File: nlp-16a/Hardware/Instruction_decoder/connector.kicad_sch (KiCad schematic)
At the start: 0 parts

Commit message: 命令デコーダ ロジック部の設計だいたい完了git statusgit statusやったぜ
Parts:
- added J? (x2): Conn_02x10_Odd_Even, Connector_PinHeader_2.54mm:PinHeader_2x10_P2.54mm_Horizontal, symbol Connector_Generic:Conn_02x10_Odd_Even
- added J? (x2): Conn_02x10_Counter_Clockwise, Connector_PinHeader_2.54mm:PinHeader_2x10_P2.54mm_Horizontal, symbol Connector_Generic:Conn_02x10_Odd_Even
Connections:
- new net 3word: J?.20 (Pin_20)
- new net ALL_CLK: J?.14 (Pin_14)
- new net A_BUS_Addr0: J?.2 (Pin_2), J?.20 (Pin_20)
- new net A_BUS_Addr1: J?.18 (Pin_18), J?.4 (Pin_4)
- new net A_BUS_Addr2: J?.16 (Pin_16), J?.6 (Pin_6)
- new net A_BUS_Addr3: J?.14 (Pin_14), J?.8 (Pin_8)
- new net BUS_A/~{B}: J?.9 (Pin_9)
- new net BUS_A/~{Y}: J?.7 (Pin_7)
- new net Fetch: J?.11 (Pin_11)
- new net GND: J?.16 (Pin_16), J?.16 (Pin_16), J?.18 (Pin_18), J?.18 (Pin_18), J?.20 (Pin_20), J?.20 (Pin_20)
- new net INT: J?.16 (Pin_16)
- new net OP0: J?.19 (Pin_19)
- new net OP1: J?.17 (Pin_17)
- new net OP2: J?.15 (Pin_15)
- new net OP3: J?.13 (Pin_13)
- new net OP4: J?.11 (Pin_11)
- new net OP5: J?.9 (Pin_9)
- new net OP6: J?.7 (Pin_7)
- new net OP7: J?.5 (Pin_5)
- new net RS: J?.14 (Pin_14)
- new net Seed_pluse: J?.12 (Pin_12)
- new net Y_BUS_Addr0: J?.12 (Pin_12), J?.2 (Pin_2)
- new net Y_BUS_Addr1: J?.10 (Pin_10), J?.4 (Pin_4)
- new net Y_BUS_Addr2: J?.6 (Pin_6), J?.8 (Pin_8)
- new net Y_BUS_Addr3: J?.6 (Pin_6), J?.8 (Pin_8)
- new net Y_Flag_sel: J?.13 (Pin_13)
- new net phi1: J?.12 (Pin_12)
- new net phi2: J?.10 (Pin_10)
- new net ~{Acc_Y}: J?.13 (Pin_13)
- new net ~{Address_Y}: J?.5 (Pin_5)
- new net ~{DEC_ALU}: J?.15 (Pin_15)
- new net ~{Flag_A}: J?.9 (Pin_9)
- new net ~{Flag_Y}: J?.9 (Pin_9)
- new net ~{INC_ALU}: J?.17 (Pin_17)
- new net ~{INTERNAL_ALU}: J?.19 (Pin_19)
- new net ~{INTERNAL_A}: J?.19 (Pin_19)
- new net ~{INTERNAL_Y}: J?.19 (Pin_19)
- new net ~{IP_A}: J?.3 (Pin_3)
- new net ~{IP_Y}: J?.3 (Pin_3)
- new net ~{IR1_Y}: J?.17 (Pin_17)
- new net ~{IR2_Y}: J?.15 (Pin_15)
- new net ~{IR3_Y}: J?.11 (Pin_11)
- new net ~{IV_A}: J?.13 (Pin_13)
- new net ~{MEM_A}: J?.7 (Pin_7)
- new net ~{MEM_Y}: J?.7 (Pin_7)
- new net ~{NOP}: J?.18 (Pin_18)
- new net ~{SP_A}: J?.1 (Pin_1)
- new net ~{SP_Y}: J?.1 (Pin_1)
- no-connect marks 0 -> 7
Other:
- note added: "YバスではΦ1，Φ2で使用する"
- note added: "Yバスでは全レジスタ指定で使用する"

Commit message: アノテーションまで完了．基板設計に入る
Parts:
- added C1, C10, C11, C12, C13, C14, C15, C16, C17, C18, C19, C2, C20, C21, C22, C23, C3, C4, C5, C6, C8, C9: C, Capacitor_THT:C_Disc_D7.5mm_W2.5mm_P5.00mm, symbol Device:C
- added C7: C_Polarized, Capacitor_THT:CP_Radial_D5.0mm_P2.50mm, symbol Device:C_Polarized
- added D1: LED, LED_THT:LED_D3.0mm, symbol Device:LED
- added H1, H2, H3, H4: MountingHole_Pad, MountingHole:MountingHole_3mm_Pad, symbol Mechanical:MountingHole_Pad
- added J3: Screw_Terminal_01x02, TerminalBlock:TerminalBlock_bornier-2_P5.08mm, symbol Connector:Screw_Terminal_01x02
- added R1: R, Resistor_SMD:R_0603_1608Metric_Pad0.98x0.95mm_HandSolder, symbol Device:R
- added U85: CD74HC00, Package_DIP:DIP-14_W7.62mm, symbol CD74HCXX:CD74HC00
- gave numbers to parts that had none: 4
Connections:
- net RS is gone; now on net ~{RS}: J2.14 (Pin_14)
- net ~{Acc_Y} is gone; now on net ~{IR3_Y}: J4.13 (Pin_13)
- net GND: now also J1.2 (Pin_2), J1.4 (Pin_4), J2.2 (Pin_2), J2.4 (Pin_4), C1.1, C10.1, C11.1, C12.1, C13.1, C14.1, C15.1, C16.1, C17.1, C18.1, C19.1, C2.1, C20.1, C21.1, C22.1, C23.1, C3.1, C4.1, C5.1, C6.1, C7.2, C8.1, C9.1, H1.1, H2.1, H3.1, H4.1, J3.1 (Pin_1), R1.2, U85.4, U85.5, U85.7 (GND), U85.7 (GND), U85.7 (GND), U85.7 (GND)
- net phi1: now also J2.10 (Pin_10)
- net phi2: now also J2.8 (Pin_8), U85.12; no longer J4.10 (Pin_10)
- net ~{IR3_Y}: no longer J4.11 (Pin_11)
- net ALL_CLK renamed ~{RS}
- net BUS_A/~{B} renamed ~{RA3}
- net BUS_A/~{Y} renamed ~{RAM_STORE->}
- net Fetch renamed ~{Fetch_Status}
- net ~{Fetch_Status}: now also U85.1
- net Seed_pluse renamed ~{Seed_pluse}
- net ~{Flag_A} renamed ~{Flag_SAVE->}
- net ~{IV_A} renamed ~{IV_JMP->}
- net ~{NOP} renamed NOP
- net NOP: now also U85.2
- new net: D1.1 (K), R1.1
- new net: U85.13, U85.3
- new net: U85.10, U85.11, U85.9
- new net Reg_pulse: J4.10 (Pin_10), U85.8
- new net VCC: C1.2, C10.2, C11.2, C12.2, C13.2, C14.2, C15.2, C16.2, C17.2, C18.2, C19.2, C2.2, C20.2, C21.2, C22.2, C23.2, C3.2, C4.2, C5.2, C6.2, C7.1, C8.2, C9.2, D1.2 (A), J3.2 (Pin_2), U85.14 (VCC), U85.14 (VCC), U85.14 (VCC), U85.14 (VCC)
- no-connect marks 7 -> 15
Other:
- note added: "BUS_A/~{B}"
- note added: "BUS_A/~{Y}"
- note added: "Power"

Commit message: 基板設計 今日はとりあえずここまで
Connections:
- net 3word: now also J2.12 (Pin_12); no longer J2.20 (Pin_20)
- net A_BUS_Addr0: now also J1.12 (Pin_12); no longer J1.20 (Pin_20)
- net A_BUS_Addr1: now also J1.10 (Pin_10); no longer J1.18 (Pin_18)
- net A_BUS_Addr2: now also J1.8 (Pin_8); no longer J1.16 (Pin_16)
- net A_BUS_Addr3: now also J1.6 (Pin_6); no longer J1.14 (Pin_14)
- net INT: now also J2.10 (Pin_10); no longer J2.16 (Pin_16)
- net NOP: now also J2.16 (Pin_16); no longer J2.18 (Pin_18)
- net Y_BUS_Addr0: now also J1.20 (Pin_20); no longer J1.12 (Pin_12)
- net Y_BUS_Addr1: now also J1.18 (Pin_18); no longer J1.10 (Pin_10)
- net Y_BUS_Addr2: now also J1.16 (Pin_16); no longer J1.8 (Pin_8)
- net Y_BUS_Addr3: now also J1.14 (Pin_14); no longer J1.6 (Pin_6)
- net phi1: now also J2.20 (Pin_20); no longer J2.10 (Pin_10)
- net phi2: now also J2.18 (Pin_18); no longer J2.8 (Pin_8)
- net ~{Seed_pluse}: now also J2.8 (Pin_8); no longer J2.12 (Pin_12)

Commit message: 基板設計 進捗
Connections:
- net 3word: now also J2.8 (Pin_8); no longer J2.12 (Pin_12)
- net ~{IR3_Y}: now also J4.11 (Pin_11); no longer J4.13 (Pin_13)
- net ~{Seed_pluse}: now also J2.12 (Pin_12); no longer J2.8 (Pin_8)
- new net Acc_Y: J4.13 (Pin_13)
- no-connect marks 15 -> 14
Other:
- note added: "Accだけは正論理"
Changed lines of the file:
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@@
   (junction (at 168.91 142.24) (diameter 0) (color 0 0 0 0)
   )
-  (no_connect (at 228.6 45.72))
   (no_connect (at 142.24 121.92))
   (no_connect (at 73.66 87.63))
@@
     (effects (font (size 1.27 1.27)) (justify left bottom))
   )
+  (text "Accだけは正論理" (at 237.49 44.45 0)
+    (effects (font (size 1.27 1.27)) (justify left bottom))
+  )
   (text "BUS_A/~{B}" (at 104.14 83.82 0)
     (effects (font (size 1.27 1.27)) (justify left bottom))
@@
     )
   )
-  (global_label "~{Seed_pluse}" (shape output) (at 62.23 85.09 180) (fields_autoplaced)
-    (effects (font (size 1.27 1.27)) (justify right))
-    (property "Intersheet References" "${INTERSHEET_REFS}" (id 0) (at 49.2336 85.0106 0)
+  (global_label "~{Seed_pluse}" (shape output) (at 62.23 80.01 180) (fields_autoplaced)
+    (effects (font (size 1.27 1.27)) (justify right))
+    (property "Intersheet References" "${INTERSHEET_REFS}" (id 0) (at 49.2336 79.9306 0)
       (effects (font (size 1.27 1.27)) (justify right) hide)
     )
@@
     )
   )
-  (global_label "~{IR3_Y}" (shape input) (at 228.6 43.18 0) (fields_autoplaced)
-    (effects (font (size 1.27 1.27)) (justify left))
-    (property "Intersheet References" "${INTERSHEET_REFS}" (id 0) (at 236.1536 43.1006 0)
+  (global_label "~{IR3_Y}" (shape input) (at 228.6 45.72 0) (fields_autoplaced)
+    (effects (font (size 1.27 1.27)) (justify left))
+    (property "Intersheet References" "${INTERSHEET_REFS}" (id 0) (at 236.1536 45.6406 0)
       (effects (font (size 1.27 1.27)) (justify left) hide)
     )
@@
     )
   )
+  (global_label "Acc_Y" (shape input) (at 228.6 43.18 0) (fields_autoplaced)
+    (effects (font (size 1.27 1.27)) (justify left))
+    (property "Intersheet References" "${INTERSHEET_REFS}" (id 0) (at 236.335 43.1006 0)
+      (effects (font (size 1.27 1.27)) (justify left) hide)
+    )
+  )
   (global_label "~{SP_Y}" (shape input) (at 228.6 58.42 0) (fields_autoplaced)
     (effects (font (size 1.27 1.27)) (justify left))
@@
     )
   )
-  (global_label "3word" (shape output) (at 62.23 80.01 180) (fields_autoplaced)
-    (effects (font (size 1.27 1.27)) (justify right))
-    (property "Intersheet References" "${INTERSHEET_REFS}" (id 0) (at 54.1926 79.9306 0)
-      (effects (font (size 1.27 1.27)) (justify right) hide)
-    )
+  (global_label "3word" (shape output) (at 62.23 85.09 180) (fields_autoplaced)
+    (effects (font (size 1.27 1.27)) (justify right))
+    (property "Intersheet References" "${INTERSHEET_REFS}" (id 0) (at 54.1926 85.0106 0)
+      (effects (font (size 1.27 1.27)) (justify right) hide)
+    )

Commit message: 命令デコーダ完了！！
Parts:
- added C23, C24, C25, C26, C27, C28, C29: C, Capacitor_THT:C_Disc_D7.0mm_W2.5mm_P5.00mm, symbol Device:C
- added D2: LED, LED_THT:LED_D3.0mm, symbol Device:LED
- added J6, J7, J8, J9: Conn_01x02_Female, Connector_PinSocket_2.54mm:PinSocket_1x02_P2.54mm_Vertical, symbol Connector:Conn_01x02_Female
- added R2: R, Resistor_SMD:R_0603_1608Metric_Pad0.98x0.95mm_HandSolder, symbol Device:R
- added U86, U87, U88: CD74HC00, Package_DIP:DIP-14_W7.62mm, symbol CD74HCXX:CD74HC00
- C1, C10, C11, C12, C13, C14, C15, C16, C17, C18, C19, C2, C20, C21, C22, C3, C4, C5, C6, C8, C9: footprint Capacitor_THT:C_Disc_D7.5mm_W2.5mm_P5.00mm -> Capacitor_THT:C_Disc_D7.0mm_W2.5mm_P5.00mm
- C7: renamed from C23; footprint Capacitor_THT:C_Disc_D7.5mm_W2.5mm_P5.00mm -> Capacitor_THT:C_Disc_D7.0mm_W2.5mm_P5.00mm
- renumbered C7 to C30
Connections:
- net GND: now also C23.1, C24.1, C25.1, C26.1, C27.1, C28.1, C29.1, J6.1 (Pin_1), J7.1 (Pin_1), J8.1 (Pin_1), J9.1 (Pin_1), R2.2, U86.7 (GND), U86.7 (GND), U86.7 (GND), U86.7 (GND), U87.7 (GND), U87.7 (GND), U87.7 (GND), U87.7 (GND), U88.7 (GND), U88.7 (GND), U88.7 (GND), U88.7 (GND); no longer U85.4, U85.5
- net VCC: now also C23.2, C24.2, C25.2, C26.2, C27.2, C28.2, C29.2, J6.2 (Pin_2), J7.2 (Pin_2), J8.2 (Pin_2), J9.2 (Pin_2), U86.14 (VCC), U86.14 (VCC), U86.14 (VCC), U86.14 (VCC), U87.14 (VCC), U87.14 (VCC), U87.14 (VCC), U87.14 (VCC), U88.14 (VCC), U88.14 (VCC), U88.14 (VCC), U88.14 (VCC)
- net phi1: now also U87.1, U87.2; no longer J4.12 (Pin_12)
- net phi2: now also U86.1, U86.2; no longer U85.12
- net INT_EN: now reaches J2.5 (Pin_5)
- net at U85.6: now also D2.2 (A)
- net at U85.10, U85.11, U85.9: now also U85.4, U85.5
- new net: U87.10, U87.12, U87.13, U87.3, U87.4, U87.5, U87.9
- new net: U86.10, U86.12, U86.13, U86.3, U86.4, U86.5, U86.9
- new net: D2.1 (K), R2.1
- new net phi1_1: U87.6
- new net phi1_2: U87.8
- new net phi1_3: J4.12 (Pin_12), U87.11
- new net phi2_1: U86.6
- new net phi2_2: U86.8
- new net phi2_3: U85.12, U86.11
- no-connect marks 14 -> 24
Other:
- moved on the sheet: C1, C10, C11, C12, C13, C14, C15, C16, C17, C18, C19, C2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

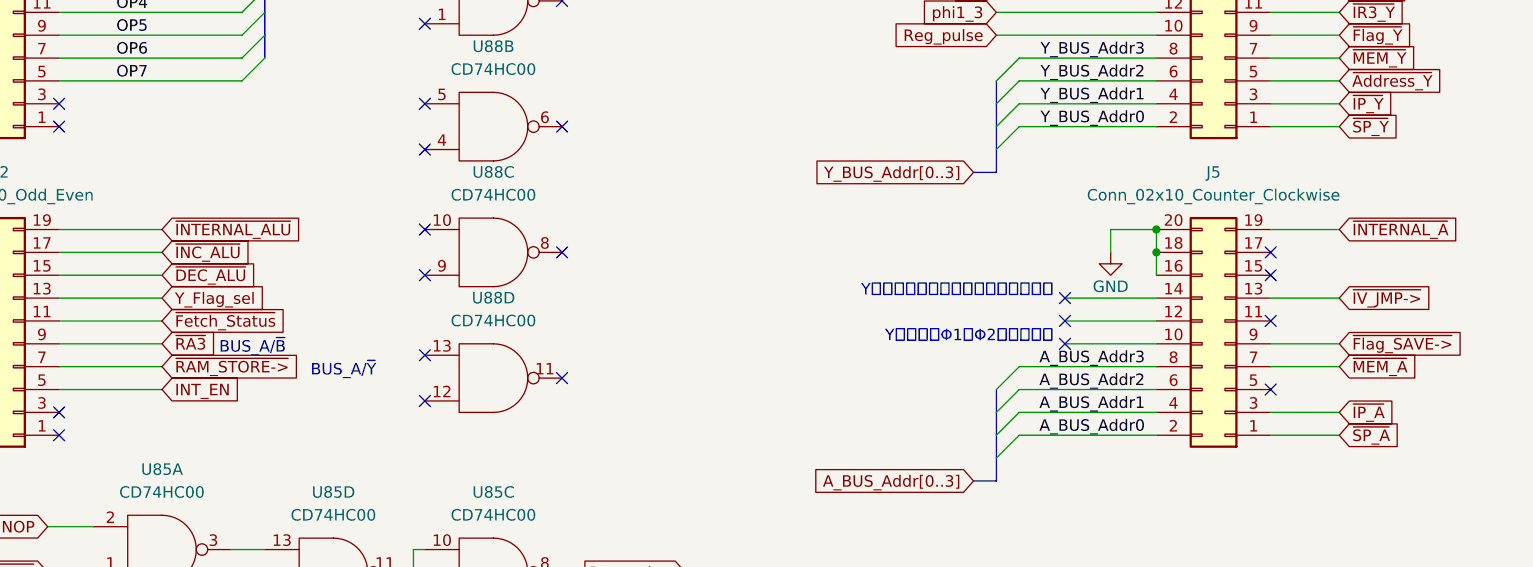
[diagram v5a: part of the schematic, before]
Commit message: 命令デコーダ修正
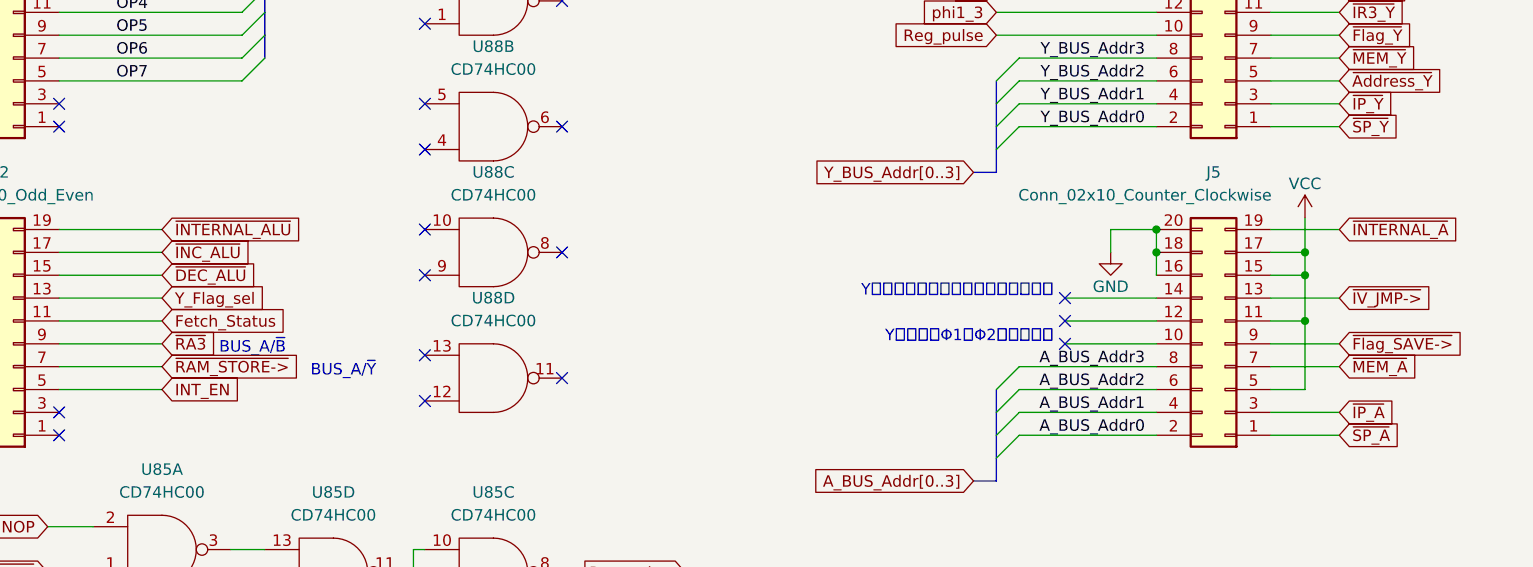
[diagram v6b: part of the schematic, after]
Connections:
- net VCC: now also J5.11 (Pin_11), J5.15 (Pin_15), J5.17 (Pin_17), J5.5 (Pin_5)
- net ~{Fetch_Status}: no longer J2.11 (Pin_11)
- new net Fetch_Status: J2.11 (Pin_11)
- no-connect marks 24 -> 20
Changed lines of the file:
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@@
   (junction (at 85.09 124.46) (diameter 0) (color 0 0 0 0)
   )
+  (junction (at 224.79 74.93) (diameter 0) (color 0 0 0 0)
+  )
   (junction (at 85.09 138.43) (diameter 0) (color 0 0 0 0)
   )
@@
   (junction (at 234.95 125.73) (diameter 0) (color 0 0 0 0)
   )
+  (junction (at 224.79 72.39) (diameter 0) (color 0 0 0 0)
+  )
   (junction (at 208.28 72.39) (diameter 0) (color 0 0 0 0)
   )
@@
   )
   (junction (at 142.24 143.51) (diameter 0) (color 0 0 0 0)
+  )
+  (junction (at 224.79 80.01) (diameter 0) (color 0 0 0 0)
   )
   (no_connect (at 142.24 44.4499))
@@
   (no_connect (at 73.66 87.63))
   (no_connect (at 198.12 77.47))
-  (no_connect (at 220.98 72.39))
-  (no_connect (at 220.98 74.93))
-  (no_connect (at 220.98 80.01))
-  (no_connect (at 220.98 87.63))
   (no_connect (at 86.36 58.42))
   (no_connect (at 86.36 55.88))
@@
     (stroke (width 0) (type default) (color 0 0 0 0))
   )
+  (wire (pts (xy 220.98 87.63) (xy 224.79 87.63))
+    (stroke (width 0) (type default) (color 0 0 0 0))
+  )
   (wire (pts (xy 62.23 181.61) (xy 59.69 181.61))
     (stroke (width 0) (type default) (color 0 0 0 0))
@@
     (stroke (width 0) (type default) (color 0 0 0 0))
   )
+  (wire (pts (xy 220.98 80.01) (xy 224.79 80.01))
+    (stroke (width 0) (type default) (color 0 0 0 0))
+  )
   (wire (pts (xy 107.95 165.1) (xy 105.41 165.1))
     (stroke (width 0) (type default) (color 0 0 0 0))
@@
     (stroke (width 0) (type default) (color 0 0 0 0))
   )
+  (wire (pts (xy 224.79 74.93) (xy 224.79 72.39))
+    (stroke (width 0) (type default) (color 0 0 0 0))
+  )
   (wire (pts (xy 52.07 50.8) (xy 73.66 50.8))
     (stroke (width 0) (type default) (color 0 0 0 0))
@@
     (stroke (width 0) (type default) (color 0 0 0 0))
   )
+  (wire (pts (xy 224.79 87.63) (xy 224.79 80.01))
+    (stroke (width 0) (type default) (color 0 0 0 0))
+  )
   (wire (pts (xy 59.69 176.53) (xy 62.23 176.53))
     (stroke (width 0) (type default) (color 0 0 0 0))
@@
     (stroke (width 0) (type default) (color 0 0 0 0))
   )
+  (wire (pts (xy 220.98 74.93) (xy 224.79 74.93))
+    (stroke (width 0) (type default) (color 0 0 0 0))
+  )
   (wire (pts (xy 167.64 158.75) (xy 176.53 158.75))
     (stroke (width 0) (type default) (color 0 0 0 0))
@@
     (stroke (width 0) (type default) (color 0 0 0 0))
   )
+  (wire (pts (xy 224.79 68.58) (xy 224.79 72.39))
+    (stroke (width 0) (type default) (color 0 0 0 0))
+  )
   (wire (pts (xy 97.79 72.39) (xy 86.36 72.39))
     (stroke (width 0) (type default) (color 0 0 0 0))
@@
     (stroke (width 0) (type default) (color 0 0 0 0))
   )
+  (wire (pts (xy 220.98 72.39) (xy 224.79 72.39))
+    (stroke (width 0) (type default) (color 0 0 0 0))
+  )
   (wire (pts (xy 229.87 135.89) (xy 238.76 135.89))
     (stroke (width 0) (type default) (color 0 0 0 0))
@@
   )
   (wire (pts (xy 234.95 125.73) (xy 228.6 125.73))
+    (stroke (width 0) (type default) (color 0 0 0 0))
+  )
+  (wire (pts (xy 224.79 80.01) (xy 224.79 74.93))
     (stroke (width 0) (type default) (color 0 0 0 0))
   )
@@
     )
   )
-  (global_label "~{Fetch_Status}" (shape input) (at 97.79 80.01 0) (fields_autoplaced)
+  (global_label "Fetch_Status" (shape input) (at 97.79 80.01 0) (fields_autoplaced)
     (effects (font (size 1.27 1.27)) (justify left))
     (property "Intersheet References" "${INTERSHEET_REFS}" (id 0) (at 112.2983 79.9306 0)
@@
     (pin "2")
   )
+  (symbol (lib_id "power:VCC") (at 224.79 68.58 0) (mirror y) (unit 1)
+    (in_bom yes) (on_board yes)
+    (property "Reference" "#PWR0101" (id 0) (at 224.79 72.39 0)
+      (effects (font (size 1.27 1.27)) hide)
+    )
+    (property "Value" "VCC" (id 1) (at 224.79 64.77 0))
+    (property "Footprint" "" (id 2) (at 224.79 68.58 0)
+      (effects (font (size 1.27 1.27)) hide)
+    )
+    (property "Datasheet" "" (id 3) (at 224.79 68.58 0)
+      (effects (font (size 1.27 1.27)) hide)
+    )
+    (pin "1")
+  )
   (symbol (lib_id "CD74HCXX:CD74HC00") (at 134.62 44.4499 0) (mirror x) (unit 1)
     (in_bom yes) (on_board yes)
@@
   )
   (symbol (lib_id "Connector_Generic:Conn_02x10_Odd_Even") (at 215.9 82.55 180) (unit 1)
-    (in_bom yes) (on_board yes) (fields_autoplaced)
+    (in_bom yes) (on_board yes)
     (property "Reference" "J5" (id 0) (at 214.63 63.5 0))
-    (property "Value" "Conn_02x10_Counter_Clockwise" (id 1) (at 214.63 66.04 0))
+    (property "Value" "Conn_02x10_Counter_Clockwise" (id 1) (at 207.01 66.04 0))
     (property "Footprint" "Connector_PinHeader_2.54mm:PinHeader_2x10_P2.54mm_Horizontal" (id 2) (at 215.9 82.55 0)
       (effects (font (size 1.27 1.27)) hide)
